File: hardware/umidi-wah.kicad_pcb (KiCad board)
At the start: 2 copper layers, 100.7 x 113.4 mm, 87 parts, among them J1 Conn_01x02, J10 Conn_02x05_Odd_Even, J11 Pots Main, J12 Pots Front, J2 Conn_01x02, J3 Conn_02x05_Odd_Even, J4 Conn_01x02, J5 Input, J6 Output, J7 Conn_02x05_Odd_Even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

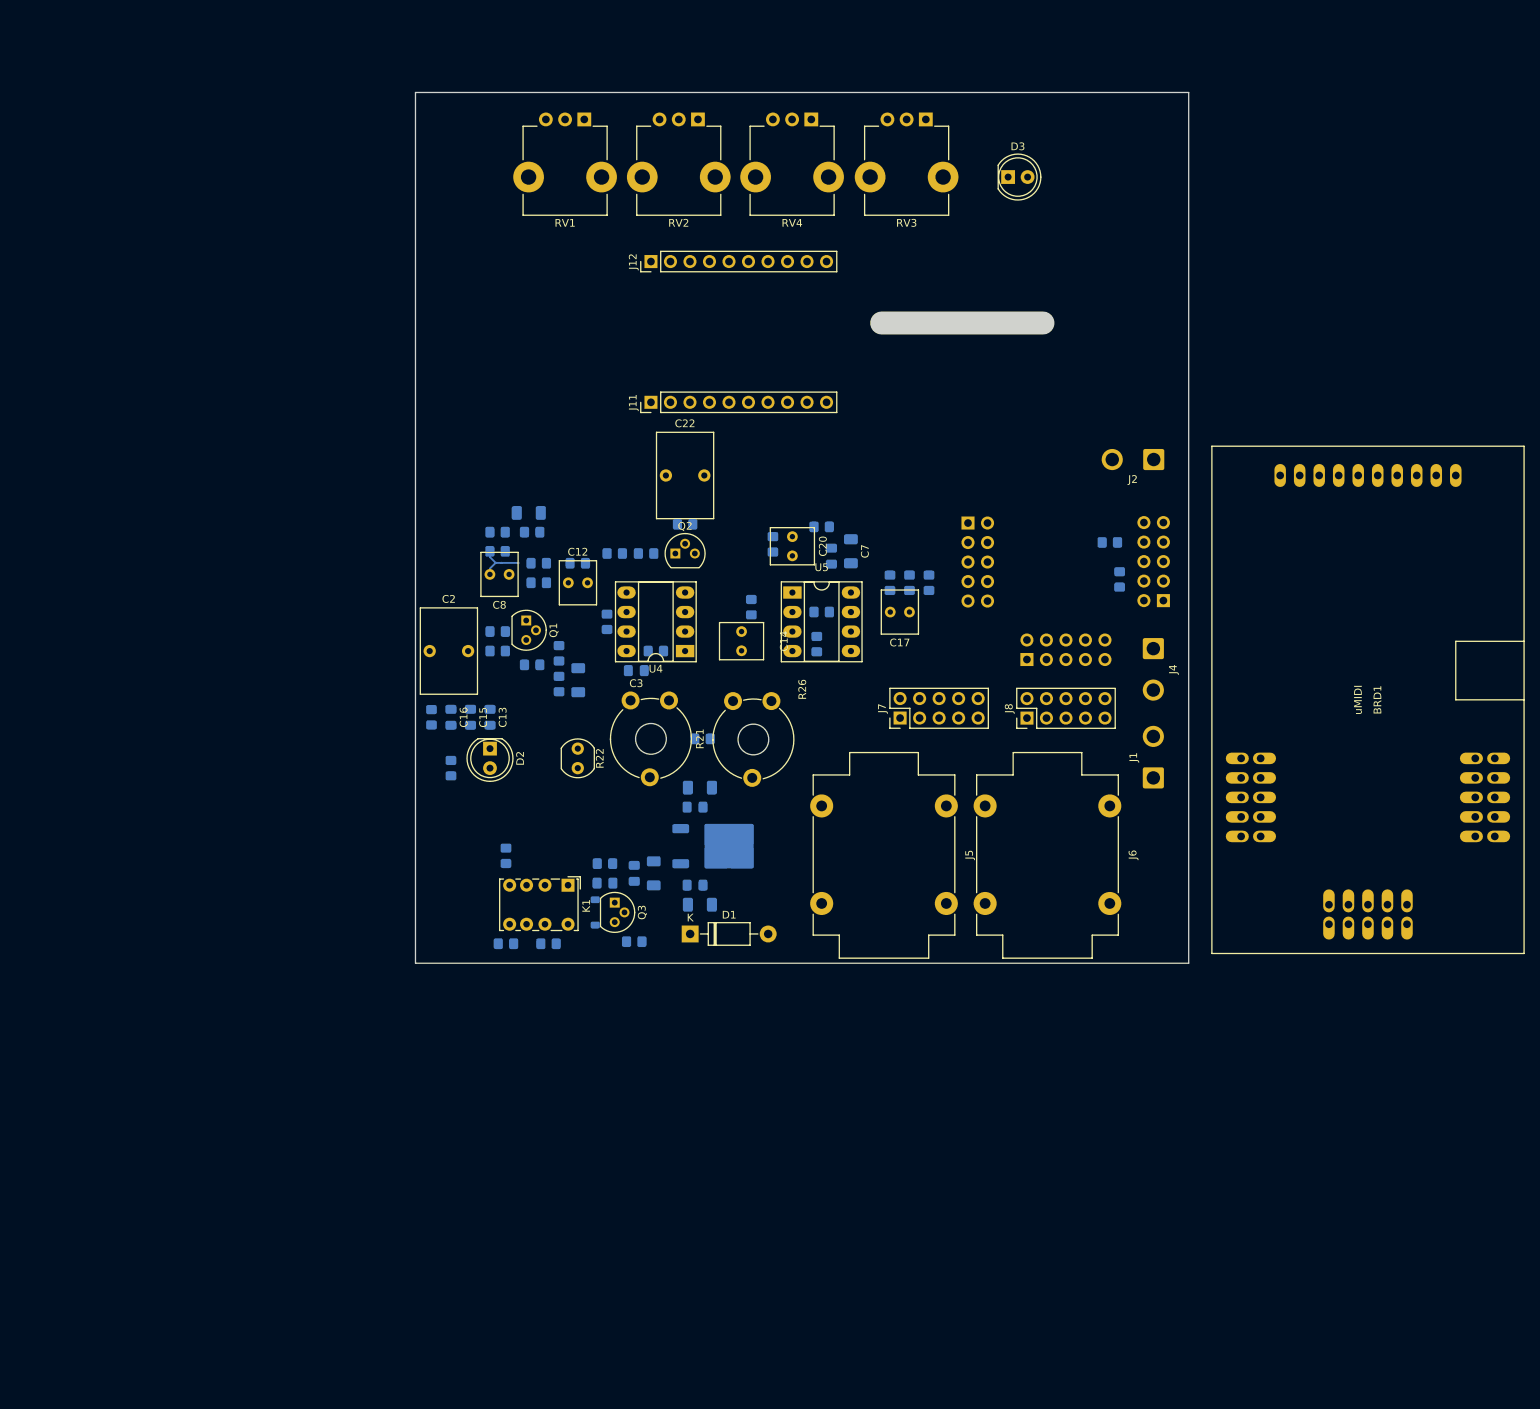
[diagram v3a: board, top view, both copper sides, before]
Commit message: Route filter circuit
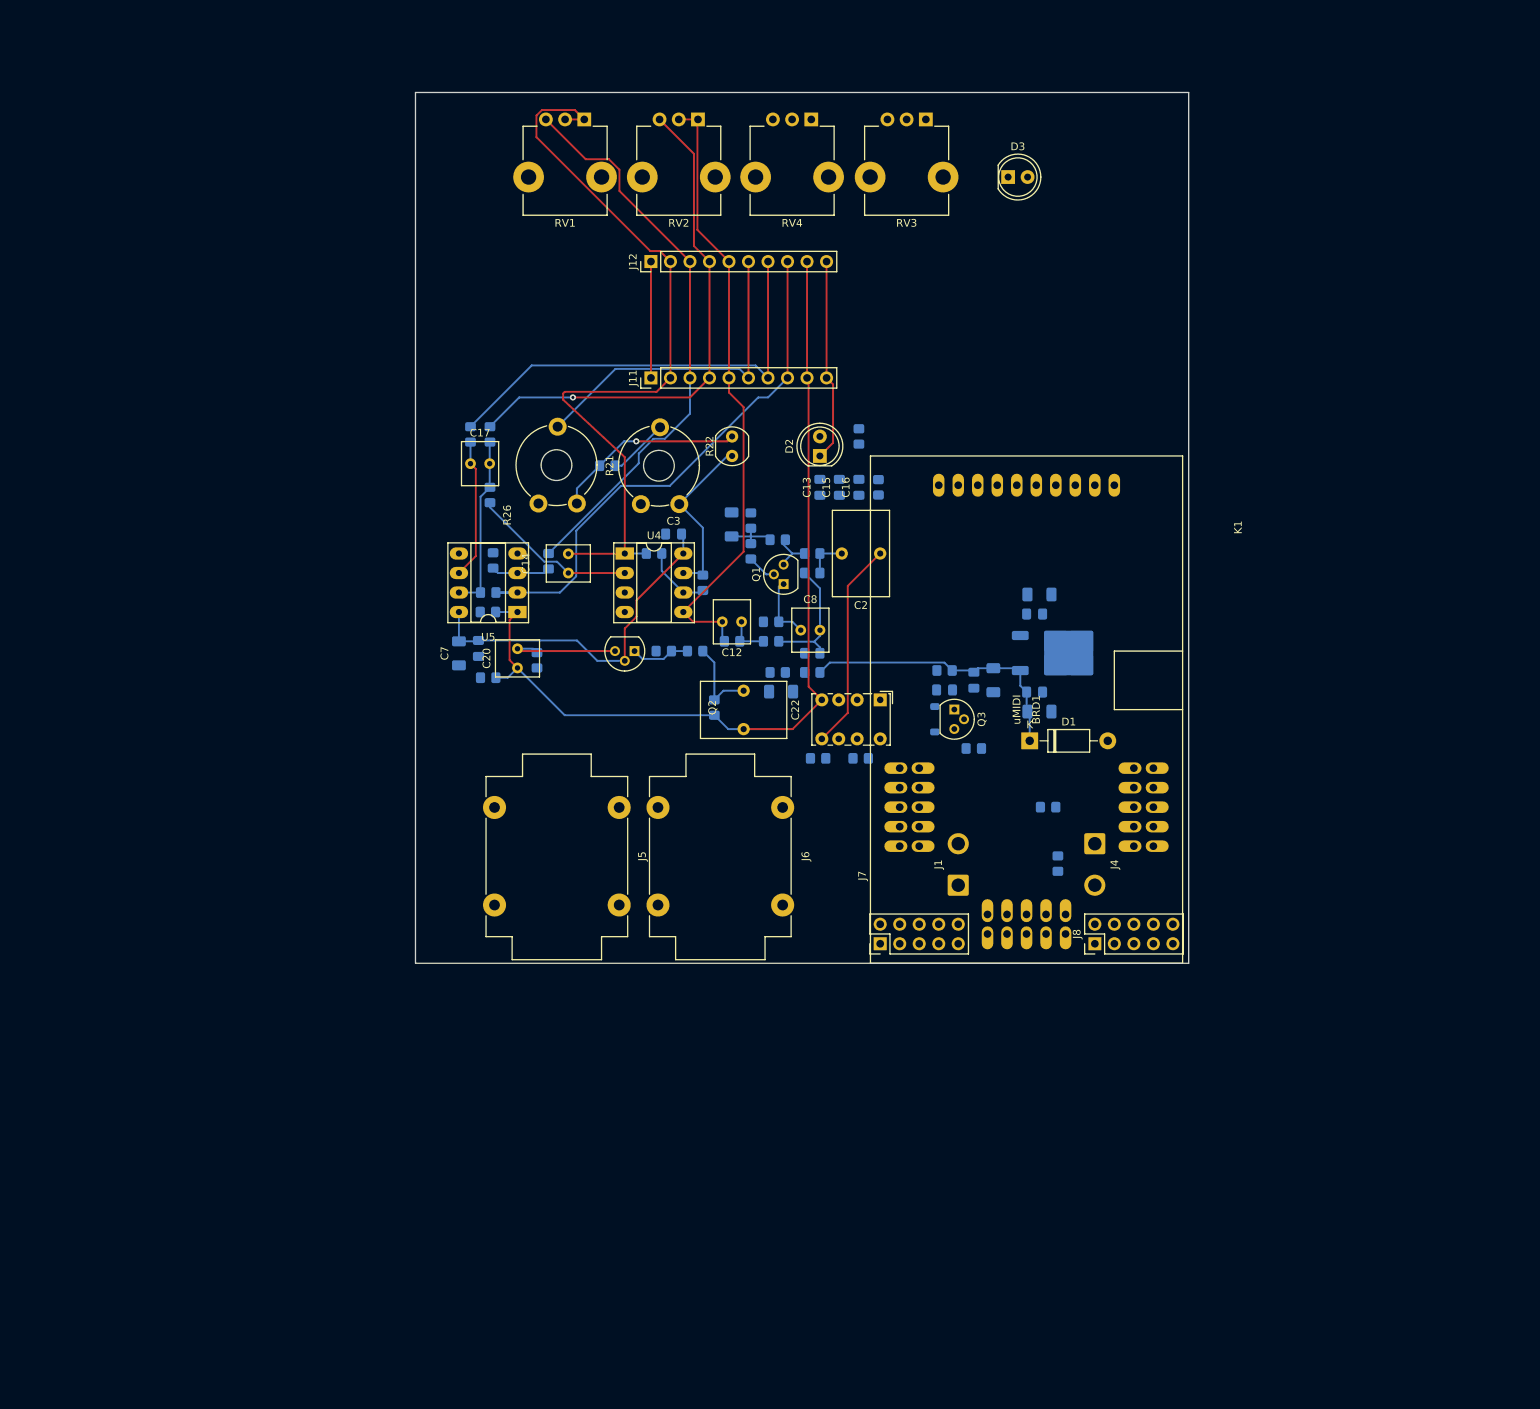
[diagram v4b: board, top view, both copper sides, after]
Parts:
- removed J10, J3, J9: Conn_02x05_Odd_Even, Connector_PinSocket_2.54mm:PinSocket_2x05_P2.54mm_Vertical
- removed J2: Conn_01x02, Connector_Wire:SolderWire-1sqmm_1x02_P5.4mm_D1.4mm_OD2.7mm
- moved R18 68.4 mm to (128.0, 64.8), turned to -90 degrees
- moved R12 65.4 mm to (130.6, 71.4), turned to -90 degrees
- moved R27 62.7 mm to (77.5, 64.5)
- moved C16 61.0 mm to (128.0, 71.4), turned to -90 degrees
- moved C17 60.3 mm to (77.5, 68.3), turned to 0 degrees
- moved C2 60.0 mm to (130.8, 80.0), turned to 180 degrees
- moved R16 57.9 mm to (80.0, 64.5)
- moved D2 57.4 mm to (123.0, 67.3), turned to 90 degrees
- moved C15 56.6 mm to (125.5, 71.4), turned to -90 degrees
- moved R14 53.3 mm to (80.0, 72.4), turned to 90 degrees
- moved C7 52.7 mm to (76.0, 93.0), turned to -90 degrees
- moved C13 52.4 mm to (123.0, 71.4), turned to -90 degrees
- moved D1 50.9 mm to (150.3, 104.4)
- moved Q3 50.9 mm to (140.5, 100.3)
- moved U3 50.9 mm to (154.1, 93.0)
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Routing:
- net /wah_out: track 0.00 -> 116.7 mm
- net /Filter/rv1_1: track 0.00 -> 101.0 mm
- net +9V: track 0.00 -> 87.3 mm
- net /Filter/rv2_1: track 0.00 -> 80.7 mm
- net /Filter/rv1_2: track 0.00 -> 75.0 mm
- net /Filter/rv3_1: track 0.00 -> 71.0 mm
- net /Filter/rv2_2: track 0.00 -> 67.5 mm, vias 0 -> 1
- net /Filter/rv4_2: track 0.00 -> 57.9 mm
- net /Filter/rv4_1: track 0.00 -> 43.6 mm
- net GND: track 0.00 -> 41.5 mm
- net /wah_in: track 0.00 -> 27.3 mm
- net Net-(R22-Pad2): track 0.00 -> 25.0 mm, vias 0 -> 1
- net Net-(C17-Pad2): track 0.00 -> 22.9 mm
- net Net-(R15-Pad2): track 0.00 -> 22.6 mm
- net Net-(U4A--): track 0.00 -> 21.7 mm
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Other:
- outline, holes or cut-outs redrawn

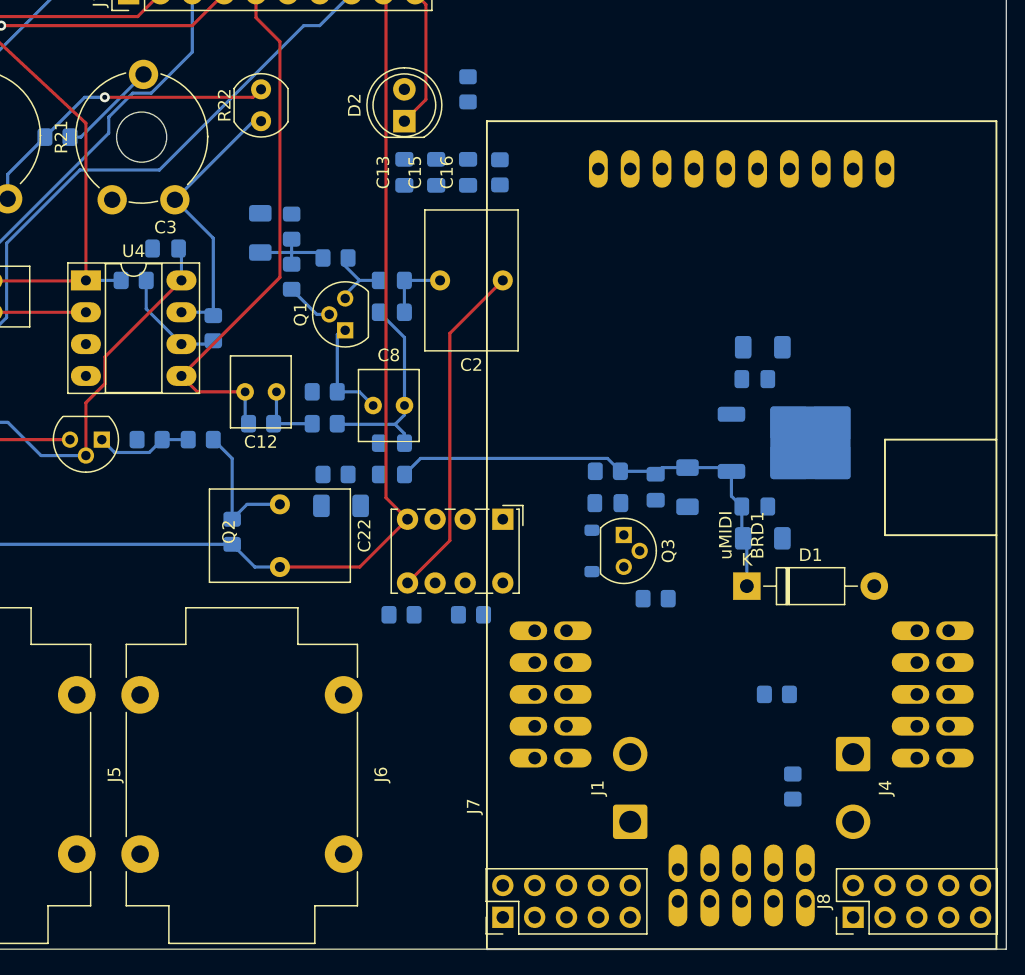
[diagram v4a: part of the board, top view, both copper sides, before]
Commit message: Route peripherals
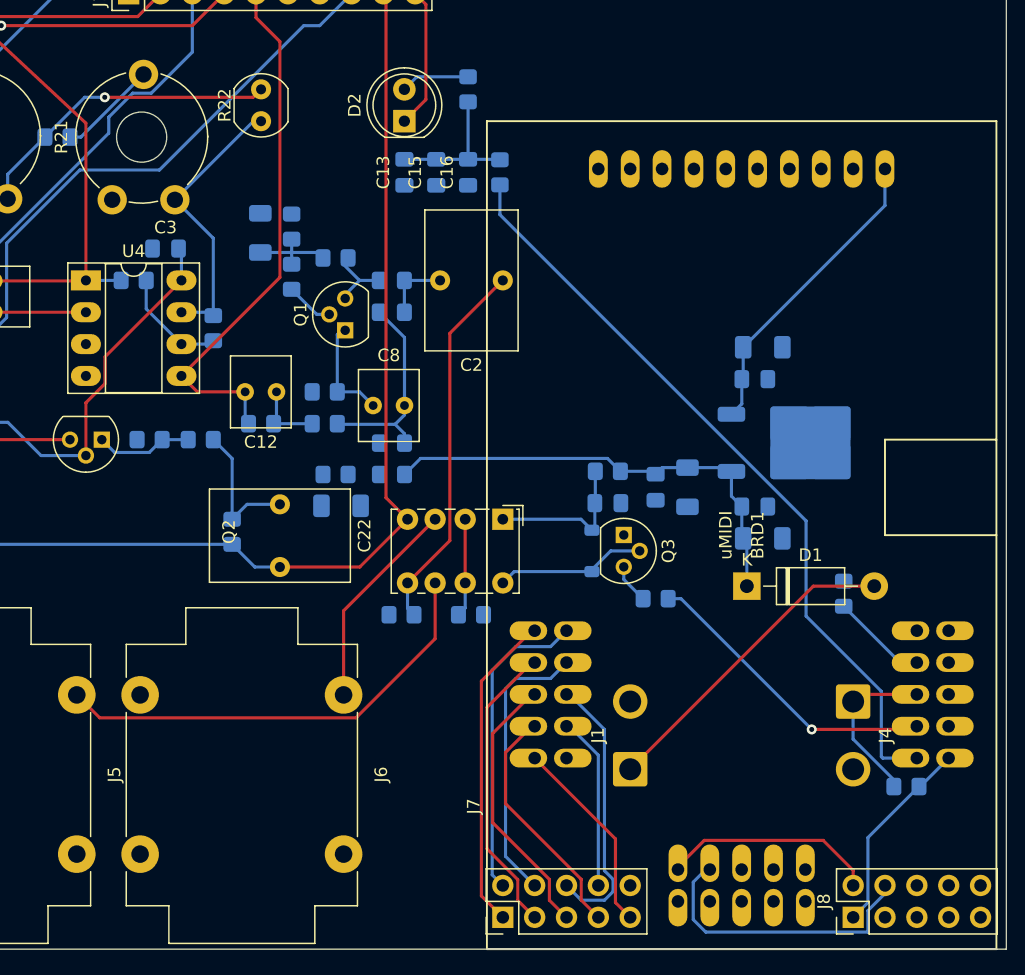
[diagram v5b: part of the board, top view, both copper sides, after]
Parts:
- moved R24 9.64 mm to (158.0, 105.0), turned to -90 degrees
- moved R25 9.06 mm to (163.0, 120.4), turned to 0 degrees
- moved J4 4.19 mm to (158.8, 113.6)
- moved J1 4.19 mm to (141.0, 119.0)
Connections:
- BRD1 pad 1: unconnected-(BRD1A-5..9V-Pad1) -> Net-(BRD1A-5..9V)
- BRD1 pad 11: unconnected-(BRD1B-VGPIO-Pad11) -> /umidi_3v3
- BRD1 pad 12: unconnected-(BRD1B-PA0(ADC0)-Pad12) -> Net-(BRD1B-PA0(ADC0))
- BRD1 pad 13: unconnected-(BRD1B-PA1(ADC1)-Pad13) -> Net-(BRD1B-PA1(ADC1))
- BRD1 pad 14: unconnected-(BRD1B-PA2(ADC2)-Pad14) -> Net-(BRD1B-PA2(ADC2))
- BRD1 pad 15: unconnected-(BRD1B-PA3(ADC3)-Pad15) -> Net-(BRD1B-PA3(ADC3))
- BRD1 pad 16: unconnected-(BRD1B-PA4(ADC4)-Pad16) -> Net-(BRD1B-PA4(ADC4))
- BRD1 pad 17: unconnected-(BRD1B-PA5(ADC5)-Pad17) -> Net-(BRD1B-PA5(ADC5))
- BRD1 pad 18: unconnected-(BRD1B-PA6(ADC6)-Pad18) -> Net-(BRD1B-PA6(ADC6))
- BRD1 pad 19: unconnected-(BRD1B-PA7(ADC7)-Pad19) -> Net-(BRD1B-PA7(ADC7))
- BRD1 pad 2: unconnected-(BRD1A-GND-Pad2) -> GND
- BRD1 pad 20: unconnected-(BRD1B-GND-Pad20) -> GND
- BRD1 pad 21: unconnected-(BRD1C-VGPIO-Pad21) -> /umidi_3v3
- BRD1 pad 22: unconnected-(BRD1C-PB0-Pad22) -> Net-(BRD1C-PB0)
- BRD1 pad 23: unconnected-(BRD1C-PB1-Pad23) -> Net-(BRD1C-PB1)
- BRD1 pad 24: unconnected-(BRD1C-PB2(DACB::DAC0)-Pad24) -> Net-(BRD1C-PB2(DACB::DAC0))
- BRD1 pad 25: unconnected-(BRD1C-PB3(DACB::DAC1)-Pad25) -> Net-(BRD1C-PB3(DACB::DAC1))
- BRD1 pad 26: unconnected-(BRD1C-PC0(SDA)-Pad26) -> Net-(BRD1C-PC0(SDA))
- BRD1 pad 27: unconnected-(BRD1C-PC1(SCL)-Pad27) -> Net-(BRD1C-PC1(SCL))
- BRD1 pad 28: unconnected-(BRD1C-PC2(C0::RXD0)-Pad28) -> Net-(BRD1C-PC2(C0::RXD0))
- BRD1 pad 29: unconnected-(BRD1C-PC3(C0::TXD0)-Pad29) -> Net-(BRD1C-PC3(C0::TXD0))
- BRD1 pad 30: unconnected-(BRD1C-GND-Pad30) -> GND
- BRD1 pad 31: unconnected-(BRD1D-VGPIO-Pad31) -> /umidi_3v3
- BRD1 pad 32: unconnected-(BRD1D-PC4(TCC1::OC1A)-Pad32) -> /led_pwm
- BRD1 pad 34: unconnected-(BRD1D-PC6(C1::RXD1)-Pad34) -> /bypass_n
- BRD1 pad 36: unconnected-(BRD1D-PD0(TCD0::OC0A)-Pad36) -> /toggle_switch
- BRD1 pad 38: unconnected-(BRD1D-PD2(TCD0::OC0C)-Pad38) -> /status_led
- BRD1 pad 40: unconnected-(BRD1D-GND-Pad40) -> GND
- C10 pad 1: Net-(J2-Pin_1) -> Net-(BRD1A-5..9V)
- C9 pad 1: Net-(J2-Pin_1) -> Net-(BRD1A-5..9V)
- J7 pad 2: Net-(J7-Pin_2) -> Net-(BRD1B-PA0(ADC0))
- J7 pad 3: Net-(J7-Pin_3) -> Net-(BRD1B-PA1(ADC1))
- J7 pad 4: Net-(J7-Pin_4) -> Net-(BRD1B-PA2(ADC2))
- J7 pad 5: Net-(J7-Pin_5) -> Net-(BRD1B-PA3(ADC3))
- J7 pad 6: Net-(J7-Pin_6) -> Net-(BRD1B-PA4(ADC4))
- J7 pad 7: Net-(J7-Pin_7) -> Net-(BRD1B-PA5(ADC5))
- J7 pad 8: Net-(J7-Pin_8) -> Net-(BRD1B-PA6(ADC6))
- J7 pad 9: Net-(J7-Pin_9) -> Net-(BRD1B-PA7(ADC7))
- J8 pad 2: Net-(J10-Pin_2) -> Net-(BRD1C-PB0)
- J8 pad 3: Net-(J10-Pin_3) -> Net-(BRD1C-PB1)
- J8 pad 4: Net-(J10-Pin_4) -> Net-(BRD1C-PB2(DACB::DAC0))
- J8 pad 5: Net-(J10-Pin_5) -> Net-(BRD1C-PB3(DACB::DAC1))
- J8 pad 6: Net-(J10-Pin_6) -> Net-(BRD1C-PC0(SDA))
- J8 pad 7: Net-(J10-Pin_7) -> Net-(BRD1C-PC1(SCL))
- J8 pad 8: Net-(J10-Pin_8) -> Net-(BRD1C-PC2(C0::RXD0))
- J8 pad 9: Net-(J10-Pin_9) -> Net-(BRD1C-PC3(C0::TXD0))
- U3 pad 3: Net-(J2-Pin_1) -> Net-(BRD1A-5..9V)
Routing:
- net /led_pwm: track 0.00 -> 61.1 mm
- net /umidi_3v3: track 0.00 -> 41.4 mm
- net Net-(J5-PadT): track 0.00 -> 36.4 mm
- net Net-(D1-A): track 0.00 -> 25.5 mm
- net /bypass_n: track 0.00 -> 24.9 mm, vias 0 -> 1
- net Net-(BRD1B-PA0(ADC0)): track 0.00 -> 24.8 mm
- net Net-(BRD1A-5..9V): track 0.00 -> 24.6 mm
- net Net-(BRD1B-PA1(ADC1)): track 0.00 -> 23.6 mm
- net Net-(BRD1C-PB2(DACB::DAC0)): track 0.00 -> 23.3 mm
- net Net-(BRD1B-PA2(ADC2)): track 0.00 -> 22.4 mm
- net Net-(BRD1B-PA4(ADC4)): track 0.00 -> 21.9 mm
- net Net-(BRD1B-PA3(ADC3)): track 0.00 -> 21.7 mm
- net Net-(BRD1B-PA5(ADC5)): track 0.00 -> 19.4 mm
- net Net-(BRD1C-PB0): track 0.00 -> 17.3 mm
- net Net-(J6-PadT): track 0.00 -> 17.0 mm
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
